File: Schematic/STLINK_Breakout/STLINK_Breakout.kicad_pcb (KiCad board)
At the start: 2 copper layers, 70 x 37 mm, 13 parts, among them J1 CN11, J2 CN3, J3 CN12, J4 To Nucleo STLINK Adapter, J5 IDC8, J6 FFC8

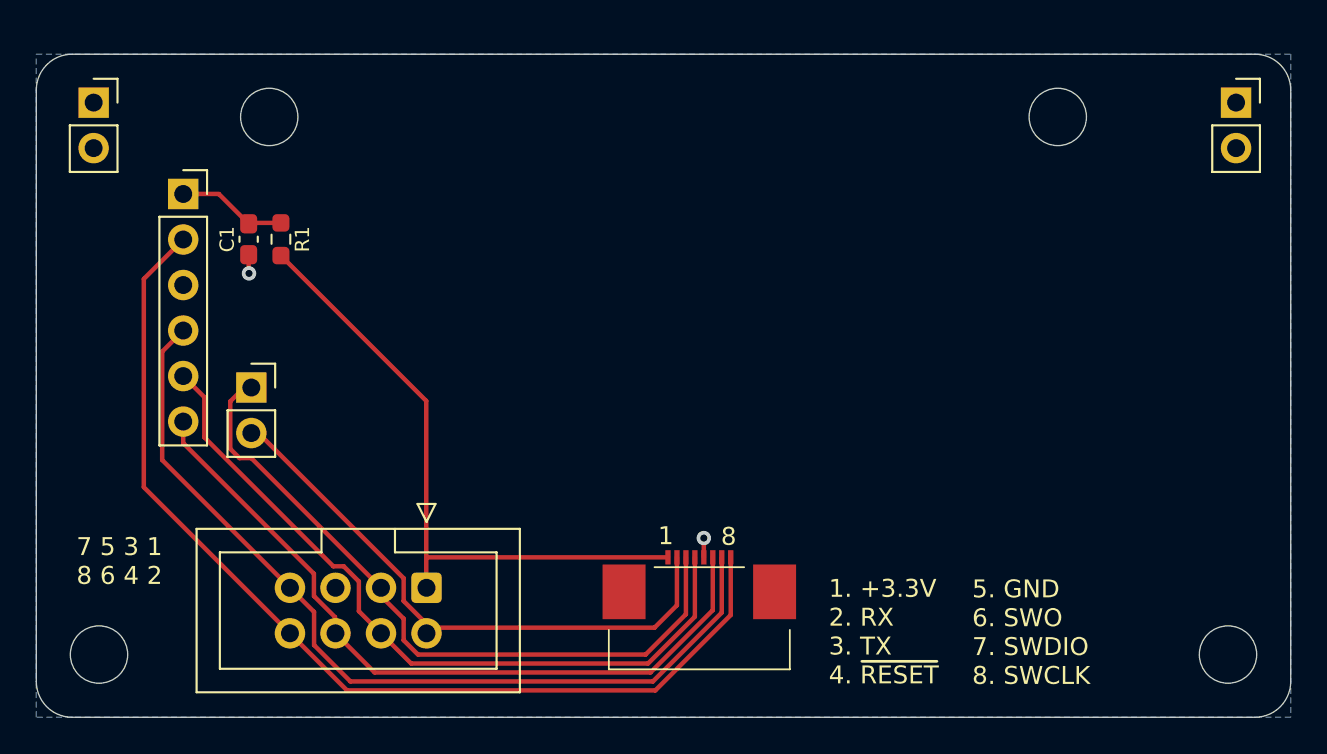
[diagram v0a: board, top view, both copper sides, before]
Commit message: Added pull-up resistor for Reset
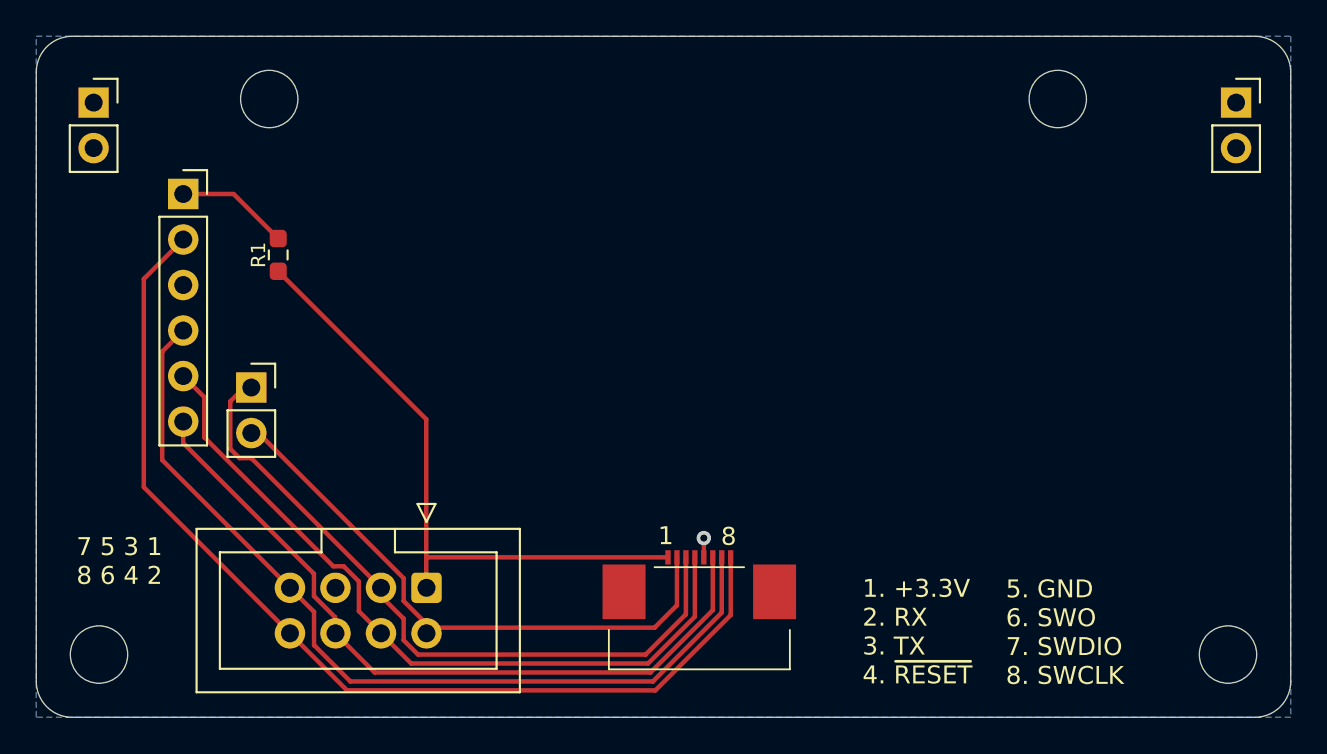
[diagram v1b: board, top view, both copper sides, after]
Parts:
- removed C1: 100nF, Capacitor_SMD:C_0603_1608Metric_Pad1.08x0.95mm_HandSolder
- R1: value 4.7kΩ -> 3kΩ
- moved H3 1.00 mm to (203.0, 72.5)
- moved H4 1.00 mm to (247.0, 72.5)
- moved R1 0.89 mm to (203.5, 81.2)
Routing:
- net GND: track 2.13 -> 1.08 mm, vias 2 -> 1
- net +3.3V: track 35.4 -> 34.6 mm
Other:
- board size 70 x 37 mm -> 70 x 38 mm
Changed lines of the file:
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@@
   )
   (paper "A4")
+  (title_block
+    (date "2023-09-09")
+  )
   (layers
     (0 "F.Cu" signal)
@@
   )
   (footprint "MountingHole:MountingHole_3.2mm_M3" (layer "F.Cu")
-    (at 203 73.5)
+    (at 203 72.5)
     (descr "Mounting Hole 3.2mm, no annular, M3")
     (tags "mounting hole 3.2mm no annular m3")
@@
   )
   (footprint "MountingHole:MountingHole_3.2mm_M3" (layer "F.Cu")
-    (at 247 73.5)
+    (at 247 72.5)
     (descr "Mounting Hole 3.2mm, no annular, M3")
     (tags "mounting hole 3.2mm no annular m3")
@@
   )
   (footprint "Resistor_SMD:R_0603_1608Metric_Pad0.98x0.95mm_HandSolder" (layer "F.Cu")
-    (at 203.65 80.325 -90)
+    (at 203.5 81.2 -90)
     (descr "Resistor SMD 0603 (1608 Metric), square (rectangular) end terminal, IPC_7351 nominal with elongated pad for handsoldering. (Body size source: IPC-SM-782 page 72, https://www.pcb-3d.com/wordpress/wp-content/uploads/ipc-sm-782a_amendment_1_and_2.pdf), generated with kicad-footprint-generator")
     (tags "resistor handsolder")
@@
     (property "ki_keywords" "R resistor")
     (attr smd)
-    (fp_text reference "R1" (at 0 -1.2 90) (layer "F.SilkS")
+    (fp_text reference "R1" (at 0 1.1 90) (layer "F.SilkS")
         (effects (font (size 0.8 0.8) (thickness 0.1)))
     )
-    (fp_text value "4.7kΩ" (at 0 1.43 90) (layer "F.Fab")
+    (fp_text value "3kΩ" (at 0 1.43 90) (layer "F.Fab")
         (effects (font (size 1 1) (thickness 0.15)))
     )
@@
       (net 8 "+3.3V") (pintype "passive"))
     (model "${KICAD6_3DMODEL_DIR}/Resistor_SMD.3dshapes/R_0603_1608Metric.wrl"
-      (offset (xyz 0 0 0))
-      (scale (xyz 1 1 1))
-      (rotate (xyz 0 0 0))
-    )
-  )
-  (footprint "Capacitor_SMD:C_0603_1608Metric_Pad1.08x0.95mm_HandSolder" (layer "F.Cu")
-    (at 201.85 80.325 -90)
-    (descr "Capacitor SMD 0603 (1608 Metric), square (rectangular) end terminal, IPC_7351 nominal with elongated pad for handsoldering. (Body size source: IPC-SM-782 page 76, https://www.pcb-3d.com/wordpress/wp-content/uploads/ipc-sm-782a_amendment_1_and_2.pdf), generated with kicad-footprint-generator")
-    (tags "capacitor handsolder")
-    (property "Sheetfile" "STLINK_Breakout.kicad_sch")
-    (property "Sheetname" "")
-    (property "ki_description" "Unpolarized capacitor, small symbol")
-    (property "ki_keywords" "capacitor cap")
-    (attr smd)
-    (fp_text reference "C1" (at 0 1.2 90) (layer "F.SilkS")
-        (effects (font (size 0.8 0.8) (thickness 0.1)))
-    )
-    (fp_text value "100nF" (at 0 1.43 90) (layer "F.Fab")
-        (effects (font (size 1 1) (thickness 0.15)))
-    )
-    (fp_text user "${REFERENCE}" (at 0 0 90) (layer "F.Fab")
-        (effects (font (size 0.4 0.4) (thickness 0.06)))
-    )
-    (fp_line (start -0.146267 -0.51) (end 0.146267 -0.51)
-      (stroke (width 0.12) (type solid)) (layer "F.SilkS"))
-    (fp_line (start -0.146267 0.51) (end 0.146267 0.51)
-      (stroke (width 0.12) (type solid)) (layer "F.SilkS"))
-    (fp_line (start -1.65 -0.73) (end 1.65 -0.73)
-      (stroke (width 0.05) (type solid)) (layer "F.CrtYd"))
-    (fp_line (start -1.65 0.73) (end -1.65 -0.73)
-      (stroke (width 0.05) (type solid)) (layer "F.CrtYd"))
-    (fp_line (start 1.65 -0.73) (end 1.65 0.73)
-      (stroke (width 0.05) (type solid)) (layer "F.CrtYd"))
-    (fp_line (start 1.65 0.73) (end -1.65 0.73)
-      (stroke (width 0.05) (type solid)) (layer "F.CrtYd"))
-    (fp_line (start -0.8 -0.4) (end 0.8 -0.4)
-      (stroke (width 0.1) (type solid)) (layer "F.Fab"))
-    (fp_line (start -0.8 0.4) (end -0.8 -0.4)
-      (stroke (width 0.1) (type solid)) (layer "F.Fab"))
-    (fp_line (start 0.8 -0.4) (end 0.8 0.4)
-      (stroke (width 0.1) (type solid)) (layer "F.Fab"))
-    (fp_line (start 0.8 0.4) (end -0.8 0.4)
-      (stroke (width 0.1) (type solid)) (layer "F.Fab"))
-    (pad "1" smd roundrect (at -0.8625 0 270) (size 1.075 0.95) (layers "F.Cu" "F.Paste" "F.Mask") (roundrect_rratio 0.25)
-      (net 9 "Net-(J4-Pin_1)") (pintype "passive"))
-    (pad "2" smd roundrect (at 0.8625 0 270) (size 1.075 0.95) (layers "F.Cu" "F.Paste" "F.Mask") (roundrect_rratio 0.25)
-      (net 1 "GND") (pintype "passive"))
-    (model "${KICAD6_3DMODEL_DIR}/Capacitor_SMD.3dshapes/C_0603_1608Metric.wrl"
       (offset (xyz 0 0 0))
       (scale (xyz 1 1 1))
@@
       (stroke (width 0) (type solid)) (fill solid) (layer "B.SilkS"))
   )
-  (gr_line (start 190 105) (end 190 72)
+  (gr_line (start 190 105) (end 190 71)
     (stroke (width 0.05) (type solid)) (layer "Edge.Cuts"))
-  (gr_line (start 192 70) (end 258 70)
+  (gr_line (start 192 69) (end 258 69)
     (stroke (width 0.05) (type solid)) (layer "Edge.Cuts"))
   (gr_arc (start 260 105) (mid 259.414214 106.414214) (end 258 107)
     (stroke (width 0.05) (type solid)) (layer "Edge.Cuts"))
-  (gr_arc (start 190 72) (mid 190.585786 70.585786) (end 192 70)
+  (gr_arc (start 190 71) (mid 190.585786 69.585786) (end 192 69)
     (stroke (width 0.05) (type solid)) (layer "Edge.Cuts"))
-  (gr_arc (start 258 70) (mid 259.414214 70.585786) (end 260 72)
+  (gr_arc (start 258 69) (mid 259.414214 69.585786) (end 260 71)
     (stroke (width 0.05) (type solid)) (layer "Edge.Cuts"))
   (gr_line (start 258 107) (end 192 107)
@@
   (gr_arc (start 192 107) (mid 190.585786 106.414214) (end 190 105)
     (stroke (width 0.05) (type solid)) (layer "Edge.Cuts"))
-  (gr_line (start 260 72) (end 260 105)
+  (gr_line (start 260 71) (end 260 105)
     (stroke (width 0.05) (type solid)) (layer "Edge.Cuts"))
   (gr_text "JLCJLCJLCJLC" (at 225 80) (layer "B.SilkS")
     (effects (font (size 0.8 0.8) (thickness 0.15)) (justify mirror))
   )
-  (gr_text locked "STLINK_Interface\nR0145_2334_Pb\nBjørner Sandom" (at 225 75.521443) (layer "B.SilkS")
+  (gr_text locked "STLINK_Interface\nR0145B_2336_Pb\nBjørner Sandom" (at 225 75.521443) (layer "B.SilkS")
     (effects (font (size 1 1) (thickness 0.15)) (justify mirror))
   )
-  (gr_text "5. GND\n6. SWO\n7. SWDIO\n8. SWCLK" (at 242.22 102.26) (layer "F.SilkS")
+  (gr_text "5. GND\n6. SWO\n7. SWDIO\n8. SWCLK" (at 244.1 102.26) (layer "F.SilkS")
     (effects (font (size 1 1) (thickness 0.15)) (justify left))
   )
@@
     (effects (font (size 1 1) (thickness 0.15)) (justify left bottom))
   )
-  (gr_text "1. +3.3V\n2. RX\n3. TX\n4. ~{RESET}" (at 234.22 102.23) (layer "F.SilkS")
+  (gr_text "1. +3.3V\n2. RX\n3. TX\n4. ~{RESET}" (at 236.1 102.23) (layer "F.SilkS")
     (effects (font (size 1 1) (thickness 0.15)) (justify left))
   )
@@
     (effects (font (size 1 1) (thickness 0.15)))
   )
-  (segment (start 201.85 82.21) (end 201.87 82.23) (width 0.25) (layer "F.Cu") (net 1))
   (segment (start 227.25 98.075) (end 227.25 97) (width 0.25) (layer "F.Cu") (net 1))
-  (segment (start 201.85 81.1875) (end 201.85 82.21) (width 0.25) (layer "F.Cu") (net 1))
-  (via (at 201.87 82.23) (size 0.8) (drill 0.4) (layers "F.Cu" "B.Cu") (net 1))
   (via (at 227.25 97) (size 0.8) (drill 0.4) (layers "F.Cu" "B.Cu") (net 1))
   (segment (start 212.04 102) (end 211.75 102.29) (width 0.25) (layer "F.Cu") (net 2))
@@
   (segment (start 207.34 105.5) (end 204.13 102.29) (width 0.25) (layer "F.Cu") (net 7))
   (segment (start 225.25 98.075) (end 211.805 98.075) (width 0.25) (layer "F.Cu") (net 8))
-  (segment (start 211.76 98.03) (end 211.76 89.3475) (width 0.25) (layer "F.Cu") (net 8))
   (segment (start 211.805 98.075) (end 211.76 98.03) (width 0.25) (layer "F.Cu") (net 8))
   (segment (start 211.76 99.76) (end 211.76 98.03) (width 0.25) (layer "F.Cu") (net 8))
   (segment (start 211.775 99.775) (end 211.76 99.76) (width 0.25) (layer "F.Cu") (net 8))
-  (segment (start 211.76 89.3475) (end 203.65 81.2375) (width 0.25) (layer "F.Cu") (net 8))
-  (segment (start 198.2 77.8) (end 200.1875 77.8) (width 0.25) (layer "F.Cu") (net 9))
-  (segment (start 201.9 79.4125) (end 201.85 79.4625) (width 0.25) (layer "F.Cu") (net 9))
-  (segment (start 203.65 79.4125) (end 201.9 79.4125) (width 0.25) (layer "F.Cu") (net 9))
-  (segment (start 200.1875 77.8) (end 201.85 79.4625) (width 0.25) (layer "F.Cu") (net 9))
+  (segment (start 211.76 90.3725) (end 203.5 82.1125) (width 0.25) (layer "F.Cu") (net 8))
+  (segment (start 211.76 98.03) (end 211.76 90.3725) (width 0.25) (layer "F.Cu") (net 8))
+  (segment (start 203.5 80.2875) (end 201.0125 77.8) (width 0.25) (layer "F.Cu") (net 9))
+  (segment (start 201.0125 77.8) (end 198.2 77.8) (width 0.25) (layer "F.Cu") (net 9))
   (zone (net 1) (net_name "GND") (layer "B.Cu") (hatch edge 0.508)
     (connect_pads (clearance 0.508))
@@
         (xy 260 107)
         (xy 190 107)
-        (xy 190 70)
-        (xy 260 70)
+        (xy 190 69)
+        (xy 260 69)
       )
     )
